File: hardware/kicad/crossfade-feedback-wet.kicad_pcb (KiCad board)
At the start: 2 copper layers, 100 x 70 mm, 12 parts, among them P301 JTR-XFADE, P302 JXF-FILT, P303 JFILT-WET, P304 JIO-WETRET, P305 JFB-INJ, P306 JXFD-PWR, P307 JXFD-CTRL, U301 OPA1679IDR

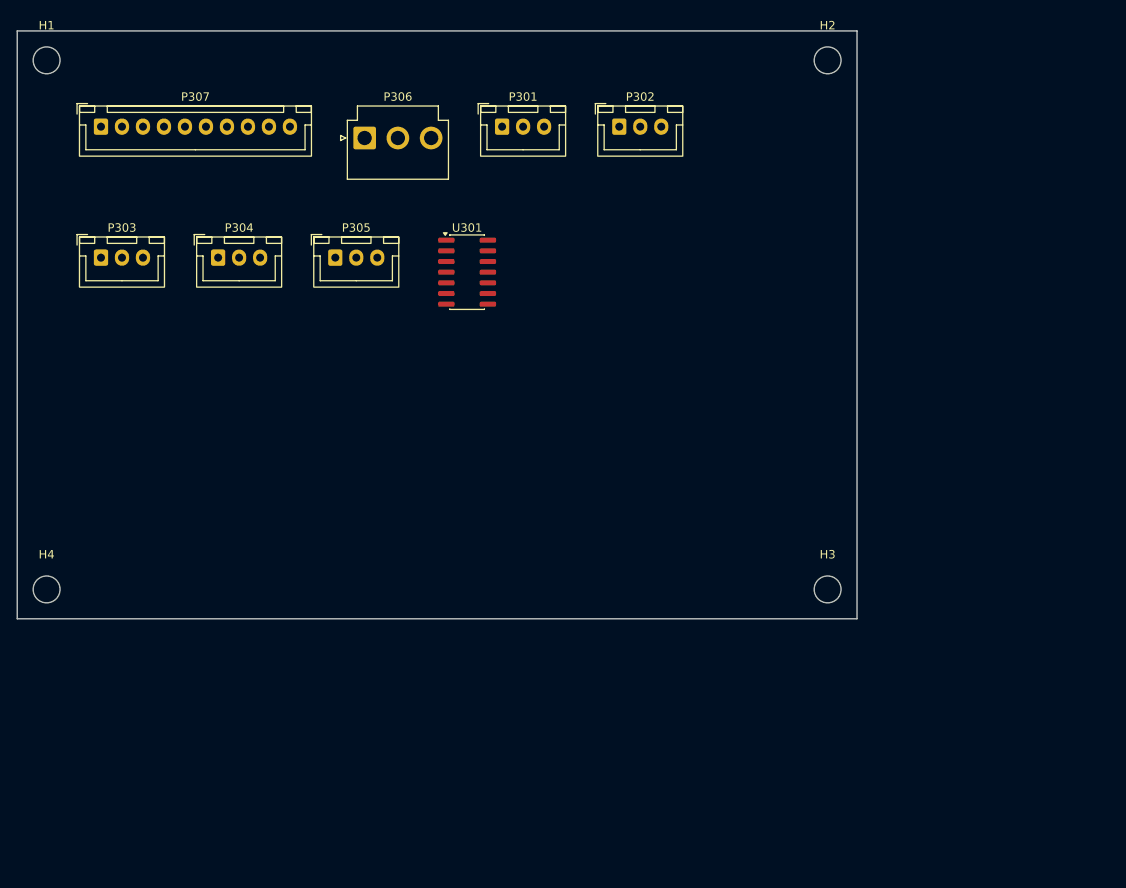
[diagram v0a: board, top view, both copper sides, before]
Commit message: Board 3 crossfade-feedback-wet: ERC 0, sim verified (crossfade/wet/feedback math exact), routed DRC 0/0, fab outputs; added K301 G5V-2 phase-select relay missing from old BOM
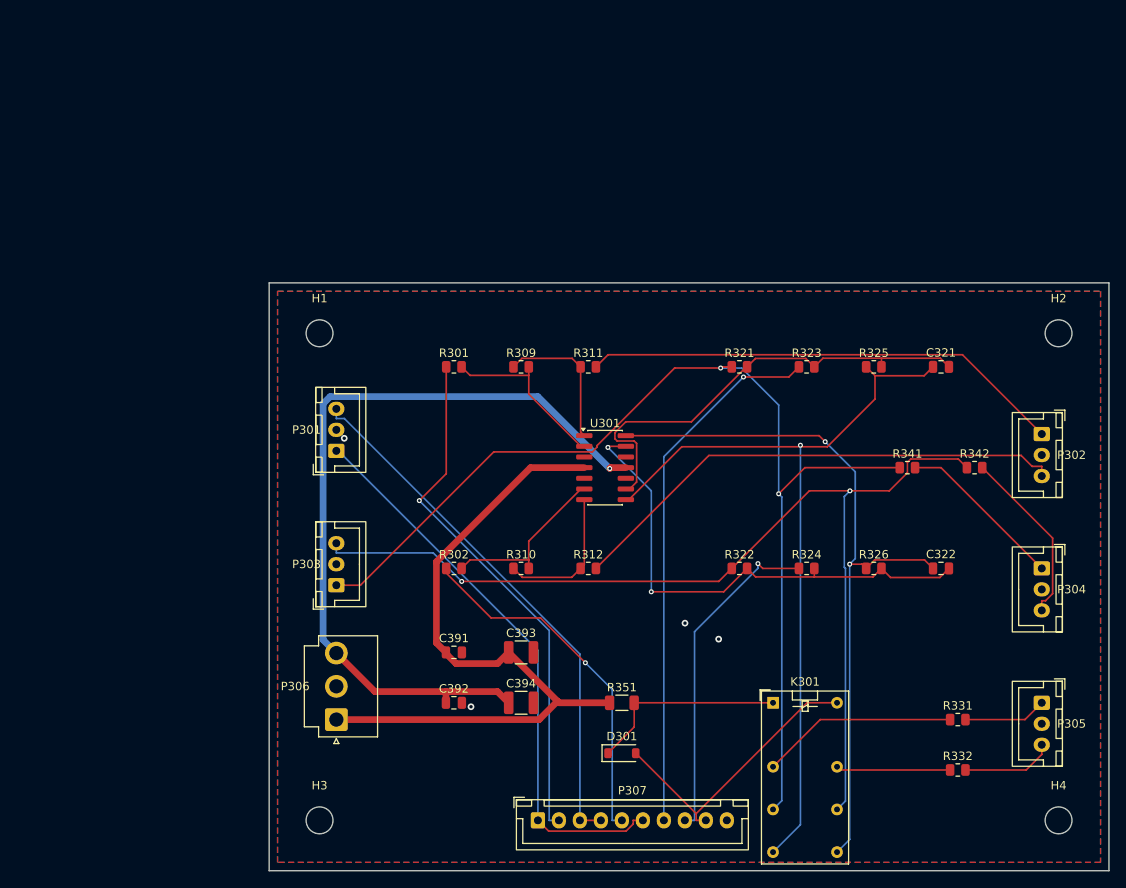
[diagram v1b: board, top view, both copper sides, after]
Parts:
- added C321: 47p, Capacitor_SMD:C_0805_2012Metric, F.Cu at (110.0, 40.0)
- added C322: 47p, Capacitor_SMD:C_0805_2012Metric, F.Cu at (110.0, 64.0)
- added C391: 100n, Capacitor_SMD:C_0805_2012Metric, F.Cu at (52.0, 74.0)
- added C392: 100n, Capacitor_SMD:C_0805_2012Metric, F.Cu at (52.0, 80.0)
- added C393: 22u, Capacitor_SMD:C_1210_3225Metric, F.Cu at (60.0, 74.0)
- added C394: 22u, Capacitor_SMD:C_1210_3225Metric, F.Cu at (60.0, 80.0)
- added D301: 1N4148W, Diode_SMD:D_SOD-123, F.Cu at (72.0, 86.0)
- added K301: G5V-2 12VDC, Relay_THT:Relay_DPDT_Omron_G5V-2, F.Cu at (90.0, 80.0)
- added R301: 20k, Resistor_SMD:R_0805_2012Metric, F.Cu at (52.0, 40.0)
- added R302: 20k, Resistor_SMD:R_0805_2012Metric, F.Cu at (52.0, 64.0)
- added R309: 20k, Resistor_SMD:R_0805_2012Metric, F.Cu at (60.0, 40.0)
- added R310: 20k, Resistor_SMD:R_0805_2012Metric, F.Cu at (60.0, 64.0)
- added R311: 100, Resistor_SMD:R_0805_2012Metric, F.Cu at (68.0, 40.0)
- added R312: 100, Resistor_SMD:R_0805_2012Metric, F.Cu at (68.0, 64.0)
- added R321: 20k, Resistor_SMD:R_0805_2012Metric, F.Cu at (86.0, 40.0)
- added R322: 20k, Resistor_SMD:R_0805_2012Metric, F.Cu at (86.0, 64.0)
- added R323: 20k, Resistor_SMD:R_0805_2012Metric, F.Cu at (94.0, 40.0)
- added R324: 20k, Resistor_SMD:R_0805_2012Metric, F.Cu at (94.0, 64.0)
- added R325: 10k, Resistor_SMD:R_0805_2012Metric, F.Cu at (102.0, 40.0)
- added R326: 10k, Resistor_SMD:R_0805_2012Metric, F.Cu at (102.0, 64.0)
- added R331: 100, Resistor_SMD:R_0805_2012Metric, F.Cu at (112.0, 82.0)
- added R332: 100, Resistor_SMD:R_0805_2012Metric, F.Cu at (112.0, 88.0)
- added R341: 100, Resistor_SMD:R_0805_2012Metric, F.Cu at (106.0, 52.0)
- added R342: 100, Resistor_SMD:R_0805_2012Metric, F.Cu at (114.0, 52.0)
- added R351: 240, Resistor_SMD:R_1206_3216Metric, F.Cu at (72.0, 80.0)
- H1, H2, H3, H4: value M3 NPTH -> M3; footprint MountingHole_3.2mm_M3 -> MountingHole:MountingHole_3.2mm_M3
- P301: value JTR-XFADE -> P301; footprint JST_XH_B3B-XH-A_1x03_P2.50mm_Vertical -> Connector_JST:JST_XH_B3B-XH-A_1x03_P2.50mm_Vertical
- P302: value JXF-FILT -> P302; footprint JST_XH_B3B-XH-A_1x03_P2.50mm_Vertical -> Connector_JST:JST_XH_B3B-XH-A_1x03_P2.50mm_Vertical
- P303: value JFILT-WET -> P303; footprint JST_XH_B3B-XH-A_1x03_P2.50mm_Vertical -> Connector_JST:JST_XH_B3B-XH-A_1x03_P2.50mm_Vertical
- P304: value JIO-WETRET -> P304; footprint JST_XH_B3B-XH-A_1x03_P2.50mm_Vertical -> Connector_JST:JST_XH_B3B-XH-A_1x03_P2.50mm_Vertical
- P305: value JFB-INJ -> P305; footprint JST_XH_B3B-XH-A_1x03_P2.50mm_Vertical -> Connector_JST:JST_XH_B3B-XH-A_1x03_P2.50mm_Vertical
- P306: value JXFD-PWR -> JXFD-PWR B3P-VH-B; footprint JST_VH_B3P-VH_1x03_P3.96mm_Vertical -> Connector_JST:JST_VH_B3P-VH_1x03_P3.96mm_Vertical
- P307: value JXFD-CTRL -> P307; footprint JST_XH_B10B-XH-A_1x10_P2.50mm_Vertical -> Connector_JST:JST_XH_B10B-XH-A_1x10_P2.50mm_Vertical
- U301: footprint SOIC-14_3.9x8.7mm_P1.27mm -> Package_SO:SOIC-14_3.9x8.7mm_P1.27mm
- moved H4 123.6 mm to (124.0, 94.0)
- moved P304 104.8 mm to (122.0, 64.0), turned to -90 degrees
- moved P305 99.4 mm to (122.0, 80.0), turned to -90 degrees
- moved P307 97.6 mm to (62.0, 94.0)
- moved P306 69.3 mm to (38.0, 82.0), turned to 90 degrees
- moved H3 66.5 mm to (36.0, 94.0)
- moved P302 62.2 mm to (122.0, 48.0), turned to -90 degrees
- moved P303 48.0 mm to (38.0, 66.0), turned to 90 degrees
- moved H1 46.0 mm to (36.0, 36.0)
- moved P301 43.4 mm to (38.0, 50.0), turned to 90 degrees
- moved H2 42.6 mm to (124.0, 36.0)
- moved U301 28.5 mm to (70.0, 52.0)
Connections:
- P301 pad 1: (no net) -> TANK_MIX_L
- P301 pad 2: (no net) -> AGND
- P301 pad 3: (no net) -> TANK_MIX_R
- P302 pad 1: (no net) -> XFADE_OUT_L
- P302 pad 2: (no net) -> AGND
- P302 pad 3: (no net) -> XFADE_OUT_R
- P303 pad 1: (no net) -> FILTCLIP_OUT_L
- P303 pad 2: (no net) -> AGND
- P303 pad 3: (no net) -> FILTCLIP_OUT_R
- P304 pad 1: (no net) -> WET_SUM_L
- P304 pad 2: (no net) -> AGND
- P304 pad 3: (no net) -> WET_SUM_R
- P305 pad 1: (no net) -> FB_RET_L
- P305 pad 2: (no net) -> AGND
- P305 pad 3: (no net) -> FB_RET_R
- P306 pad 1: (no net) -> +15VA
- P306 pad 2: (no net) -> AGND
- P306 pad 3: (no net) -> -15VA
- P307 pad 1: (no net) -> TANK_MIX_L
- P307 pad 10: (no net) -> AGND
- P307 pad 2: (no net) -> XFD_L_WIPER
- P307 pad 3: (no net) -> TANK_MIX_R
- P307 pad 4: (no net) -> TANK_MIX_R
- P307 pad 5: (no net) -> XFD_R_WIPER
- P307 pad 6: (no net) -> TANK_MIX_L
- P307 pad 7: (no net) -> FB_L_WIPER
- P307 pad 8: (no net) -> FB_R_WIPER
- P307 pad 9: (no net) -> CTL_FB_INV
- U301 pad 1: (no net) -> XFADE_SUM_L
- U301 pad 10: (no net) -> AGND
- U301 pad 11: (no net) -> -15VA
- U301 pad 12: (no net) -> AGND
- U301 pad 13: (no net) -> N_FB_R_M
- U301 pad 14: (no net) -> FB_INV_R
- U301 pad 2: (no net) -> N_XF_L_M
- U301 pad 3: (no net) -> AGND
- U301 pad 4: (no net) -> +15VA
- U301 pad 5: (no net) -> AGND
- U301 pad 6: (no net) -> N_XF_R_M
- U301 pad 7: (no net) -> XFADE_SUM_R
- U301 pad 8: (no net) -> FB_INV_L
- U301 pad 9: (no net) -> N_FB_L_M
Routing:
- net FILTCLIP_OUT_L: track 0.00 -> 131.2 mm, vias 0 -> 2
- net FILTCLIP_OUT_R: track 0.00 -> 123.5 mm, vias 0 -> 2
- net FB_INV_L: track 0.00 -> 96.2 mm, vias 0 -> 1
- net -15VA: track 0.00 -> 94.7 mm, vias 0 -> 1
- net FB_INV_R: track 0.00 -> 86.3 mm, vias 0 -> 2
- net +15VA: track 0.00 -> 83.9 mm
- net TANK_MIX_L: track 0.00 -> 67.9 mm
- net TANK_MIX_R: track 0.00 -> 64.1 mm
- net FB_L_WIPER: track 0.00 -> 63.8 mm, vias 0 -> 1
- net XFD_L_WIPER: track 0.00 -> 62.9 mm, vias 0 -> 1
- net N_FB_R_M: track 0.00 -> 60.9 mm, vias 0 -> 2
- net XFADE_OUT_R: track 0.00 -> 60.3 mm
- net XFADE_OUT_L: track 0.00 -> 57.6 mm
- net N_FB_L_M: track 0.00 -> 55.5 mm
- net XFD_R_WIPER: track 0.00 -> 42.8 mm, vias 0 -> 1
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- added copper zone on B.Cu, net AGND
- added copper zone on F.Cu, net AGND
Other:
- board text removed: "GAS Rev A - Crossfade / Feedback / Wet Board"
- board text removed: "OUTLINE SCAFFOLD - NOT FOR FAB"
